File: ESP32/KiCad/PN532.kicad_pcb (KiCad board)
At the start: 2 copper layers, 42 x 42 mm, 33 parts, among them J1 Header, J2 SPOX, U1 PN532

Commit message: Closer - not quite tracked yet
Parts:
- added J3: MiniGrid, RevK:Connector-MilliGrid-2x2, F.Cu at (121.0, 79.0)
- added X1: 27.12MHz, Crystal:Crystal_SMD_2016-4Pin_2.0x1.6mm, F.Cu at (127.5, 73.5)
- U1: footprint Package_DFN_QFN:QFN-40-1EP_6x6mm_P0.5mm_EP4.6x4.6mm -> RevK:QFN-40-(hand)-1EP_6x6mm_P0.5mm_EP4.6x4.6mm
- moved C14 34.1 mm to (118.1, 83.8), turned to 180 degrees
- moved J1 31.7 mm to (117.4, 87.0)
- moved C8 30.6 mm to (128.4, 68.4)
- moved C17 29.3 mm to (119.2, 73.0), turned to 270 degrees
- moved C15 28.0 mm to (123.4, 71.4), turned to 180 degrees
- moved C6 27.7 mm to (134.1, 71.4)
- moved L2 27.7 mm to (132.9, 75.1)
- moved C2 27.5 mm to (136.7, 76.6)
- moved J2 27.4 mm to (117.4, 88.4)
- moved U1 27.4 mm to (127.0, 78.7)
- moved C5 27.4 mm to (134.1, 86.6)
- moved A1 27.3 mm to (100.0, 58.0)
- moved R3 27.3 mm to (130.8, 89.6)
- moved R4 27.3 mm to (130.8, 92.0)
- moved C3 27.2 mm to (136.7, 84.0)
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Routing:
- net +3V3: track 0.00 -> 71.0 mm, vias 0 -> 2
- net GND: track 0.00 -> 68.8 mm, vias 0 -> 12
- net +5V: track 0.00 -> 38.3 mm, vias 0 -> 2
- net Net-(J1-Pad3): track 0.00 -> 16.4 mm
- net Net-(J1-Pad4): track 0.00 -> 14.2 mm
- net Net-(R3-Pad1): track 0.00 -> 12.3 mm
- net Net-(C10-Pad1): track 0.00 -> 11.6 mm
- net Net-(R7-Pad1): track 0.00 -> 11.2 mm, vias 0 -> 2
- net Net-(C8-Pad1): track 0.00 -> 10.9 mm, vias 0 -> 2
- net Net-(C4-Pad2): track 0.00 -> 8.83 mm
- net Net-(C15-Pad1): track 0.00 -> 8.34 mm
- net Net-(C16-Pad1): track 0.00 -> 5.71 mm
- net Net-(C3-Pad1): track 0.00 -> 4.70 mm
- net Net-(A1-Pad3): track 0.00 -> 4.12 mm
- net Net-(A1-Pad1): track 0.00 -> 4.12 mm
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- added copper zone on B.Cu, net GND

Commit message: Tracked...
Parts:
- added D4: RED, LED_THT:LED_D3.0mm, B.Cu at (108.1, 66.0)
- added D5: AMBER, LED_THT:LED_D3.0mm, B.Cu at (108.1, 70.6)
- added D6: GREEN, LED_THT:LED_D3.0mm, B.Cu at (108.1, 75.2)
- added SW1: TAMPER, Button_Switch_THT:SW_PUSH_6mm, F.Cu at (112.8, 84.4)
- moved D3 3.20 mm to (109.5, 75.2)
- moved R7 3.20 mm to (114.5, 75.2)
- moved D2 1.60 mm to (109.5, 70.6)
- moved R6 1.60 mm to (114.5, 70.6)
- moved C13 0.77 mm to (128.8, 84.4)
- moved C14 0.64 mm to (117.8, 84.4)
- moved C12 0.61 mm to (123.1, 84.4)
- moved C11 0.20 mm to (115.8, 80.0)
- moved C7 0.20 mm to (115.8, 77.6)
- moved D1 0.10 mm to (109.5, 66.0)
- moved R5 0.10 mm to (114.5, 66.0)
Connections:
- U1 pad 25: Net-(R7-Pad1) -> Net-(U1-Pad25)
- U1 pad 29: Net-(R6-Pad1) -> Net-(U1-Pad29)
- U1 pad 30: Net-(R5-Pad1) -> Net-(U1-Pad30)
- U1 pad 32: Net-(U1-Pad32) -> Net-(R5-Pad1)
- U1 pad 33: Net-(U1-Pad33) -> Net-(R6-Pad1)
- U1 pad 34: Net-(U1-Pad34) -> Net-(R7-Pad1)
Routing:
- net Net-(SW1-Pad2): track 0.00 -> 26.1 mm, vias 0 -> 2
- net Net-(R6-Pad1): track 0.00 -> 24.6 mm, vias 0 -> 2
- net Net-(R5-Pad1): track 0.45 -> 23.7 mm, vias 0 -> 2
- net GND: track 68.8 -> 89.8 mm
- net +3V3: track 71.0 -> 89.9 mm
- net Net-(R7-Pad1): track 11.2 -> 22.0 mm
- net Net-(J1-Pad3): track 16.4 -> 25.7 mm, vias 0 -> 1
- net Net-(J1-Pad4): track 14.2 -> 17.5 mm
- net +5V: track 38.3 -> 39.9 mm

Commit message: Tidy tracks
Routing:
- net GND: track 89.8 -> 81.4 mm
- net Net-(R5-Pad1): track 23.7 -> 27.9 mm
- net +3V3: track 89.9 -> 87.1 mm
- net Net-(J1-Pad3): track 25.7 -> 27.4 mm
- net +5V: track 39.9 -> 38.7 mm
- net Net-(J1-Pad4): track 17.5 -> 16.9 mm
- net Net-(SW1-Pad2): track 26.1 -> 25.6 mm

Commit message: Tracked, and pretty much ready to try it.
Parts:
- removed D4: RED, LED_THT:LED_D3.0mm
- removed D5: AMBER, LED_THT:LED_D3.0mm
- removed D6: GREEN, LED_THT:LED_D3.0mm
- added H1: MountingHole, MountingHole:MountingHole_4.3mm_M4, F.Cu at (135.0, 65.0)
- added H2: MountingHole, MountingHole:MountingHole_4.3mm_M4, F.Cu at (107.0, 93.0)
- D1, D2, D3: footprint LED_SMD:LED_1206_3216Metric_Castellated -> RevK:LED_D3.0mm_and_SMD
- X1: value 27.12MHz -> 27.12MHz (Mouser 830053099); footprint Crystal:Crystal_SMD_2016-4Pin_2.0x1.6mm -> RevK:Crystal-3.4x2.7
- moved SW1 25.1 mm to (136.0, 94.0), turned to 180 degrees
- moved R4 20.3 mm to (112.8, 82.8)
- moved R3 18.6 mm to (112.8, 85.2)
- moved C15 7.02 mm to (130.3, 72.5), turned to 90 degrees
- moved R2 6.26 mm to (122.5, 68.7)
- moved R1 5.57 mm to (128.7, 67.5), turned to 90 degrees
- moved C10 4.56 mm to (121.5, 73.2), turned to 270 degrees
- moved R5 3.79 mm to (115.3, 69.7)
- moved D3 2.84 mm to (110.0, 78.0)
- moved D2 2.45 mm to (110.0, 73.0)
- moved C8 2.34 mm to (126.3, 67.4), turned to 270 degrees
- moved D1 2.06 mm to (110.0, 68.0)
- moved R6 1.70 mm to (115.3, 72.1)
- moved C16 1.46 mm to (123.9, 72.4), turned to 90 degrees
- moved R7 1.06 mm to (115.3, 74.5)
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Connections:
- J3 pad 3: Net-(J1-Pad4) -> Net-(J1-Pad3)
- J3 pad 4: Net-(J1-Pad3) -> Net-(J1-Pad4)
- U1 pad 27: Net-(J1-Pad4) -> Net-(J1-Pad3)
- U1 pad 28: Net-(J1-Pad3) -> Net-(J1-Pad4)
- U1 pad 32: Net-(R5-Pad1) -> Net-(R7-Pad1)
- U1 pad 34: Net-(R7-Pad1) -> Net-(R5-Pad1)
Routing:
- net Net-(R3-Pad1): track 12.3 -> 27.5 mm
- net +3V3: track 87.1 -> 78.3 mm
- net Net-(C10-Pad1): track 11.6 -> 20.0 mm, vias 0 -> 2
- net +5V: track 38.7 -> 45.3 mm
- net Net-(C8-Pad1): track 10.9 -> 17.3 mm
- net Net-(C16-Pad1): track 5.71 -> 11.2 mm
- net Net-(R7-Pad1): track 22.4 -> 18.0 mm
- net GND: track 81.4 -> 85.5 mm, vias 12 -> 11
- net Net-(J1-Pad3): track 27.4 -> 24.3 mm, vias 1 -> 0
- net Net-(C4-Pad2): track 8.83 -> 11.8 mm
- net Net-(SW1-Pad2): track 25.6 -> 22.8 mm
- net Net-(D3-Pad2): track 2.05 -> 4.55 mm
- net Net-(R6-Pad1): track 24.7 -> 22.2 mm
- net Net-(C15-Pad1): track 8.34 -> 6.71 mm
- net Net-(D1-Pad2): track 2.05 -> 3.23 mm
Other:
- board text added: "A"
- board text added: "G"
- board text added: "GND"
- board text added: "R"
- board text added: "RX"
- board text added: "TX"
- board text added: "VCC"
- board text added: "www.me.uk"

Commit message: As ordered from PCB Train today...
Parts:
- H1, H2: footprint MountingHole:MountingHole_4.3mm_M4 -> MountingHole:MountingHole_3.2mm_M3_Pad_Via
- moved H1 1.41 mm to (134.0, 66.0)
- moved H2 1.41 mm to (108.0, 92.0)
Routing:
- net +5V: track 45.3 -> 40.6 mm
- net Net-(C4-Pad2): track 11.8 -> 12.9 mm

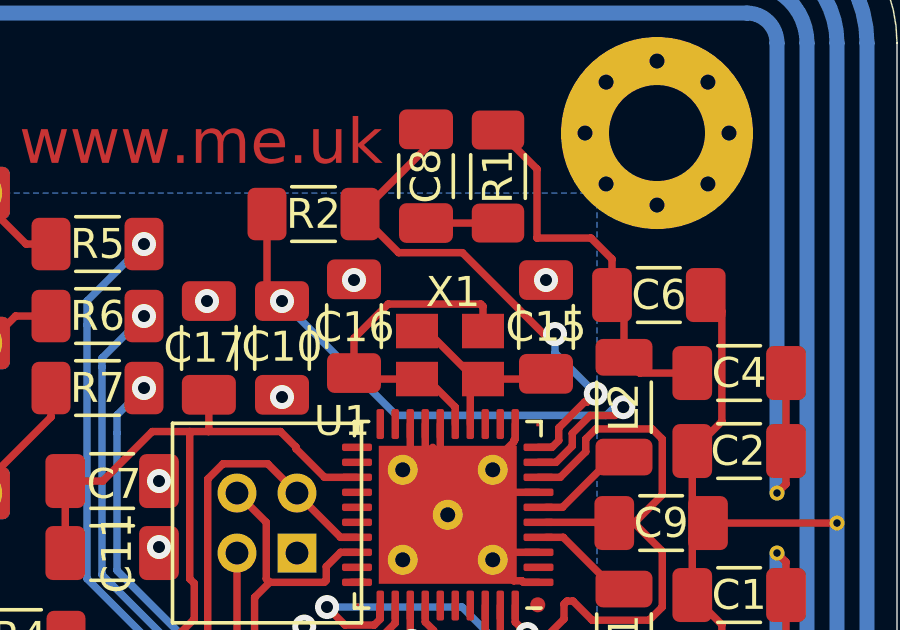
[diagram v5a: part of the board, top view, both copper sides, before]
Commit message: Fixed crystal
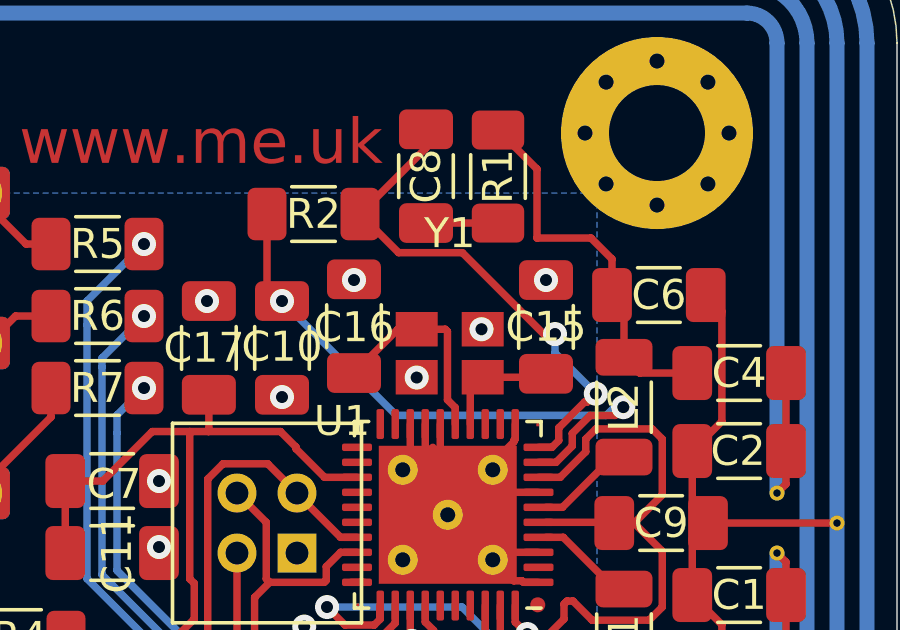
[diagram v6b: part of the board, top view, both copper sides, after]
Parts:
- removed X1: 27.12MHz (Mouser 830053099), RevK:Crystal-3.4x2.7
- added Y1: 27.12MHz (Mouser 830053099), RevK:Crystal-3.4x2.7, F.Cu at (127.1, 73.3)
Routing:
- net Net-(C16-Pad1): track 11.2 -> 6.94 mm
- net Net-(C15-Pad1): track 6.71 -> 3.89 mm
- net GND: vias 11 -> 13
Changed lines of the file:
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@@
     (thickness 1.6)
     (drawings 30)
-    (tracks 322)
+    (tracks 318)
     (zones 0)
     (modules 38)
@@
     (add_net "Net-(U1-Pad37)")
   )
+  (module RevK:Crystal-3.4x2.7 (layer F.Cu)
+    (at 127.09 73.34 180)
+    (fp_text reference Y1 (at 0 4) (layer F.SilkS)
+      (effects (font (size 1 1) (thickness 0.15)))
+    )
+    (fp_text value "27.12MHz (Mouser 830053099)" (at 0 2.5) (layer F.Fab)
+      (effects (font (size 1 1) (thickness 0.15)))
+    )
+    (fp_line (start -1.7 1.35) (end -1.7 -1.35) (layer F.CrtYd) (width 0.12))
+    (fp_line (start -1.7 -1.35) (end 1.7 -1.35) (layer F.CrtYd) (width 0.12))
+    (fp_line (start 1.7 -1.35) (end 1.7 1.35) (layer F.CrtYd) (width 0.12))
+    (fp_line (start 1.7 1.35) (end -1.7 1.35) (layer F.CrtYd) (width 0.12))
+    (pad 2 smd rect (at 1.1 -0.8 180) (size 1.4 1.15) (layers F.Cu F.Paste F.Mask)
+      (net 1 GND))
+    (pad 3 smd rect (at 1.1 0.8 180) (size 1.4 1.15) (layers F.Cu F.Paste F.Mask)
+      (net 11 "Net-(C16-Pad1)"))
+    (pad 4 smd rect (at -1.1 0.8 180) (size 1.4 1.15) (layers F.Cu F.Paste F.Mask)
+      (net 1 GND))
+    (pad 1 smd rect (at -1.1 -0.8 180) (size 1.4 1.15) (layers F.Cu F.Paste F.Mask)
+      (net 10 "Net-(C15-Pad1)"))
+  )
   (module MountingHole:MountingHole_3.2mm_M3_Pad_Via (layer F.Cu)
     (at 108 92)
@@
       (effects (font (size 1 1) (thickness 0.15)))
     )
-    (fp_text user %R (at 0.3 0) (layer F.Fab)
-      (effects (font (size 1 1) (thickness 0.15)))
-    )
     (fp_circle (center 0 0) (end 3.2 0) (layer Cmts.User) (width 0.15))
     (fp_circle (center 0 0) (end 3.45 0) (layer F.CrtYd) (width 0.05))
+    (fp_text user %R (at 0.3 0) (layer F.Fab)
+      (effects (font (size 1 1) (thickness 0.15)))
+    )
     (pad 1 thru_hole circle (at 1.697056 -1.697056) (size 0.8 0.8) (drill 0.5) (layers *.Cu *.Mask))
     (pad 1 thru_hole circle (at 0 -2.4) (size 0.8 0.8) (drill 0.5) (layers *.Cu *.Mask))
@@
       (effects (font (size 1 1) (thickness 0.15)))
     )
-    (fp_text user %R (at 0.3 0) (layer F.Fab)
-      (effects (font (size 1 1) (thickness 0.15)))
-    )
     (fp_circle (center 0 0) (end 3.2 0) (layer Cmts.User) (width 0.15))
     (fp_circle (center 0 0) (end 3.45 0) (layer F.CrtYd) (width 0.05))
+    (fp_text user %R (at 0.3 0) (layer F.Fab)
+      (effects (font (size 1 1) (thickness 0.15)))
+    )
     (pad 1 thru_hole circle (at 1.697056 -1.697056) (size 0.8 0.8) (drill 0.5) (layers *.Cu *.Mask))
     (pad 1 thru_hole circle (at 0 -2.4) (size 0.8 0.8) (drill 0.5) (layers *.Cu *.Mask))
@@
     (pad 1 thru_hole circle (at 2.4 0) (size 0.8 0.8) (drill 0.5) (layers *.Cu *.Mask))
     (pad 1 thru_hole circle (at 0 0) (size 6.4 6.4) (drill 3.2) (layers *.Cu *.Mask))
-  )
-  (module RevK:Crystal-3.4x2.7 (layer F.Cu)
-    (at 127.1 73.4 180)
-    (fp_text reference X1 (at -0.1 2.1 180) (layer F.SilkS)
-      (effects (font (size 1 1) (thickness 0.15)))
-    )
-    (fp_text value "27.12MHz (Mouser 830053099)" (at 0 2.5) (layer F.Fab)
-      (effects (font (size 1 1) (thickness 0.15)))
-    )
-    (fp_line (start 1.7 1.35) (end -1.7 1.35) (layer F.CrtYd) (width 0.12))
-    (fp_line (start 1.7 -1.35) (end 1.7 1.35) (layer F.CrtYd) (width 0.12))
-    (fp_line (start -1.7 -1.35) (end 1.7 -1.35) (layer F.CrtYd) (width 0.12))
-    (fp_line (start -1.7 1.35) (end -1.7 -1.35) (layer F.CrtYd) (width 0.12))
-    (pad 2 smd rect (at 1.1 -0.8 180) (size 1.4 1.15) (layers F.Cu F.Paste F.Mask)
-      (net 11 "Net-(C16-Pad1)"))
-    (pad 1 smd rect (at 1.1 0.8 180) (size 1.4 1.15) (layers F.Cu F.Paste F.Mask)
-      (net 10 "Net-(C15-Pad1)"))
-    (pad 2 smd rect (at -1.1 0.8 180) (size 1.4 1.15) (layers F.Cu F.Paste F.Mask)
-      (net 11 "Net-(C16-Pad1)"))
-    (pad 1 smd rect (at -1.1 -0.8 180) (size 1.4 1.15) (layers F.Cu F.Paste F.Mask)
-      (net 10 "Net-(C15-Pad1)"))
   )
   (module RevK:PN532-Antenna (layer B.Cu)
@@
   (segment (start 111.2 85.2) (end 111.2 86.4) (width 0.25) (layer B.Cu) (net 9))
   (segment (start 119.9 90.6) (end 115.4 90.6) (width 0.25) (layer B.Cu) (net 9))
-  (segment (start 127.775 74.625) (end 128.2 74.2) (width 0.25) (layer F.Cu) (net 10))
-  (segment (start 127.775 75.7) (end 127.775 74.625) (width 0.25) (layer F.Cu) (net 10))
-  (segment (start 130.125 74.2) (end 130.3 74.025) (width 0.25) (layer F.Cu) (net 10))
-  (segment (start 128.2 74.2) (end 130.125 74.2) (width 0.25) (layer F.Cu) (net 10))
-  (segment (start 127.939998 74.2) (end 128.2 74.2) (width 0.25) (layer F.Cu) (net 10))
-  (segment (start 126.339998 72.6) (end 127.939998 74.2) (width 0.25) (layer F.Cu) (net 10))
-  (segment (start 126 72.6) (end 126.339998 72.6) (width 0.25) (layer F.Cu) (net 10))
-  (segment (start 126.339998 74.2) (end 126 74.2) (width 0.25) (layer F.Cu) (net 11))
-  (segment (start 127.275 75.135002) (end 126.339998 74.2) (width 0.25) (layer F.Cu) (net 11))
-  (segment (start 127.275 75.7) (end 127.275 75.135002) (width 0.25) (layer F.Cu) (net 11))
-  (segment (start 124.1 74.2) (end 123.9 74) (width 0.25) (layer F.Cu) (net 11))
-  (segment (start 126 74.2) (end 124.1 74.2) (width 0.25) (layer F.Cu) (net 11))
-  (segment (start 123.9 72.839998) (end 123.9 74) (width 0.25) (layer F.Cu) (net 11))
-  (segment (start 125.039999 71.699999) (end 123.9 72.839998) (width 0.25) (layer F.Cu) (net 11))
-  (segment (start 128.124999 71.699999) (end 125.039999 71.699999) (width 0.25) (layer F.Cu) (net 11))
-  (segment (start 128.2 71.775) (end 128.124999 71.699999) (width 0.25) (layer F.Cu) (net 11))
-  (segment (start 128.2 72.6) (end 128.2 71.775) (width 0.25) (layer F.Cu) (net 11))
   (segment (start 114.3 82.8) (end 114.3 85.2) (width 0.25) (layer F.Cu) (net 12))
   (segment (start 128.275 81.75) (end 128.275 85.325) (width 0.25) (layer F.Cu) (net 12))
@@
   (segment (start 129.8 86.7) (end 129.8 89.2) (width 0.25) (layer F.Cu) (net 36))
   (segment (start 124.25 80.975) (end 123.799998 80.975) (width 0.25) (layer F.Cu) (net 37) (status 30))
+  (via (at 128.15 72.54) (size 0.8) (drill 0.4) (layers F.Cu B.Cu) (net 1))
+  (via (at 125.99 74.15) (size 0.8) (drill 0.4) (layers F.Cu B.Cu) (net 1))
+  (segment (start 127.775 74.555) (end 128.19 74.14) (width 0.25) (layer F.Cu) (net 10))
+  (segment (start 127.775 75.7) (end 127.775 74.555) (width 0.25) (layer F.Cu) (net 10))
+  (segment (start 130.185 74.14) (end 130.3 74.025) (width 0.25) (layer F.Cu) (net 10))
+  (segment (start 128.19 74.14) (end 130.185 74.14) (width 0.25) (layer F.Cu) (net 10))
+  (segment (start 125.36 72.54) (end 123.9 74) (width 0.25) (layer F.Cu) (net 11))
+  (segment (start 125.99 72.54) (end 125.36 72.54) (width 0.25) (layer F.Cu) (net 11))
+  (segment (start 127.275 75.151978) (end 127.275 75.7) (width 0.25) (layer F.Cu) (net 11))
+  (segment (start 127.015001 74.891979) (end 127.275 75.151978) (width 0.25) (layer F.Cu) (net 11))
+  (segment (start 126.94 72.54) (end 127.015001 72.615001) (width 0.25) (layer F.Cu) (net 11))
+  (segment (start 127.015001 72.615001) (end 127.015001 74.891979) (width 0.25) (layer F.Cu) (net 11))
+  (segment (start 125.99 72.54) (end 126.94 72.54) (width 0.25) (layer F.Cu) (net 11))
   (zone (net 1) (net_name GND) (layer B.Cu) (hatch edge 0.508)
     (connect_pads (clearance 0.508))

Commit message: Tweak tracks
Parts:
- moved R1 0.10 mm to (128.7, 67.3)
- moved C6 0.10 mm to (134.2, 71.4)
- moved C8 0.10 mm to (126.3, 67.3)
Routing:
- net Net-(C4-Pad2): track 12.9 -> 10.4 mm
- net Net-(C8-Pad1): track 17.3 -> 18.9 mm, vias 2 -> 0

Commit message: Refined tracks.
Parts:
- moved A1 29.7 mm to (121.0, 79.0)
- moved R2 5.10 mm to (117.5, 68.7)
- moved C8 3.99 mm to (122.5, 68.7), turned to 0 degrees
- moved R3 2.32 mm to (113.0, 87.5), turned to 270 degrees
- moved R5 2.00 mm to (115.5, 71.7)
- moved R6 2.00 mm to (115.5, 74.1)
- moved R7 2.00 mm to (115.5, 76.5)
- moved R1 1.64 mm to (127.7, 68.7), turned to 0 degrees
- moved C11 1.46 mm to (115.4, 81.4)
- moved C7 1.46 mm to (115.4, 79.0)
- moved C9 1.33 mm to (135.5, 79.0)
- moved R4 1.00 mm to (112.7, 83.8)
- moved C5 0.78 mm to (134.9, 86.6)
- moved C6 0.78 mm to (134.9, 71.4)
- moved C3 0.20 mm to (136.7, 83.8)
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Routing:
- net GND: track 85.5 -> 92.4 mm
- net +5V: track 40.6 -> 36.5 mm
- net Net-(D1-Pad2): track 3.23 -> 6.70 mm
- net Net-(D2-Pad2): track 2.46 -> 5.75 mm
- net Net-(C10-Pad1): track 20.0 -> 22.7 mm
- net Net-(C8-Pad1): track 18.9 -> 20.8 mm
- net Net-(R7-Pad1): track 18.0 -> 16.2 mm
- net Net-(A1-Pad3): track 4.12 -> 2.65 mm
- net Net-(A1-Pad1): track 4.12 -> 2.65 mm
- net Net-(D3-Pad2): track 4.55 -> 5.79 mm
- net Net-(R5-Pad1): track 27.4 -> 28.5 mm
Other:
- board text added: "Tamper"
